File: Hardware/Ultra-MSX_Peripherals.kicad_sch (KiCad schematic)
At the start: 56 parts, among them J4 OST_Conn_302-S341, J5 Amphenol_L17H1220134, J6 DIN-8_SDF-80J, J7 AdamTech_USB3-2_USB_C_Recepta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, J8 SDF-130J, J9 Ultra-av-daughter, Q2 MMBT2907AM3T5G, U16 LM211

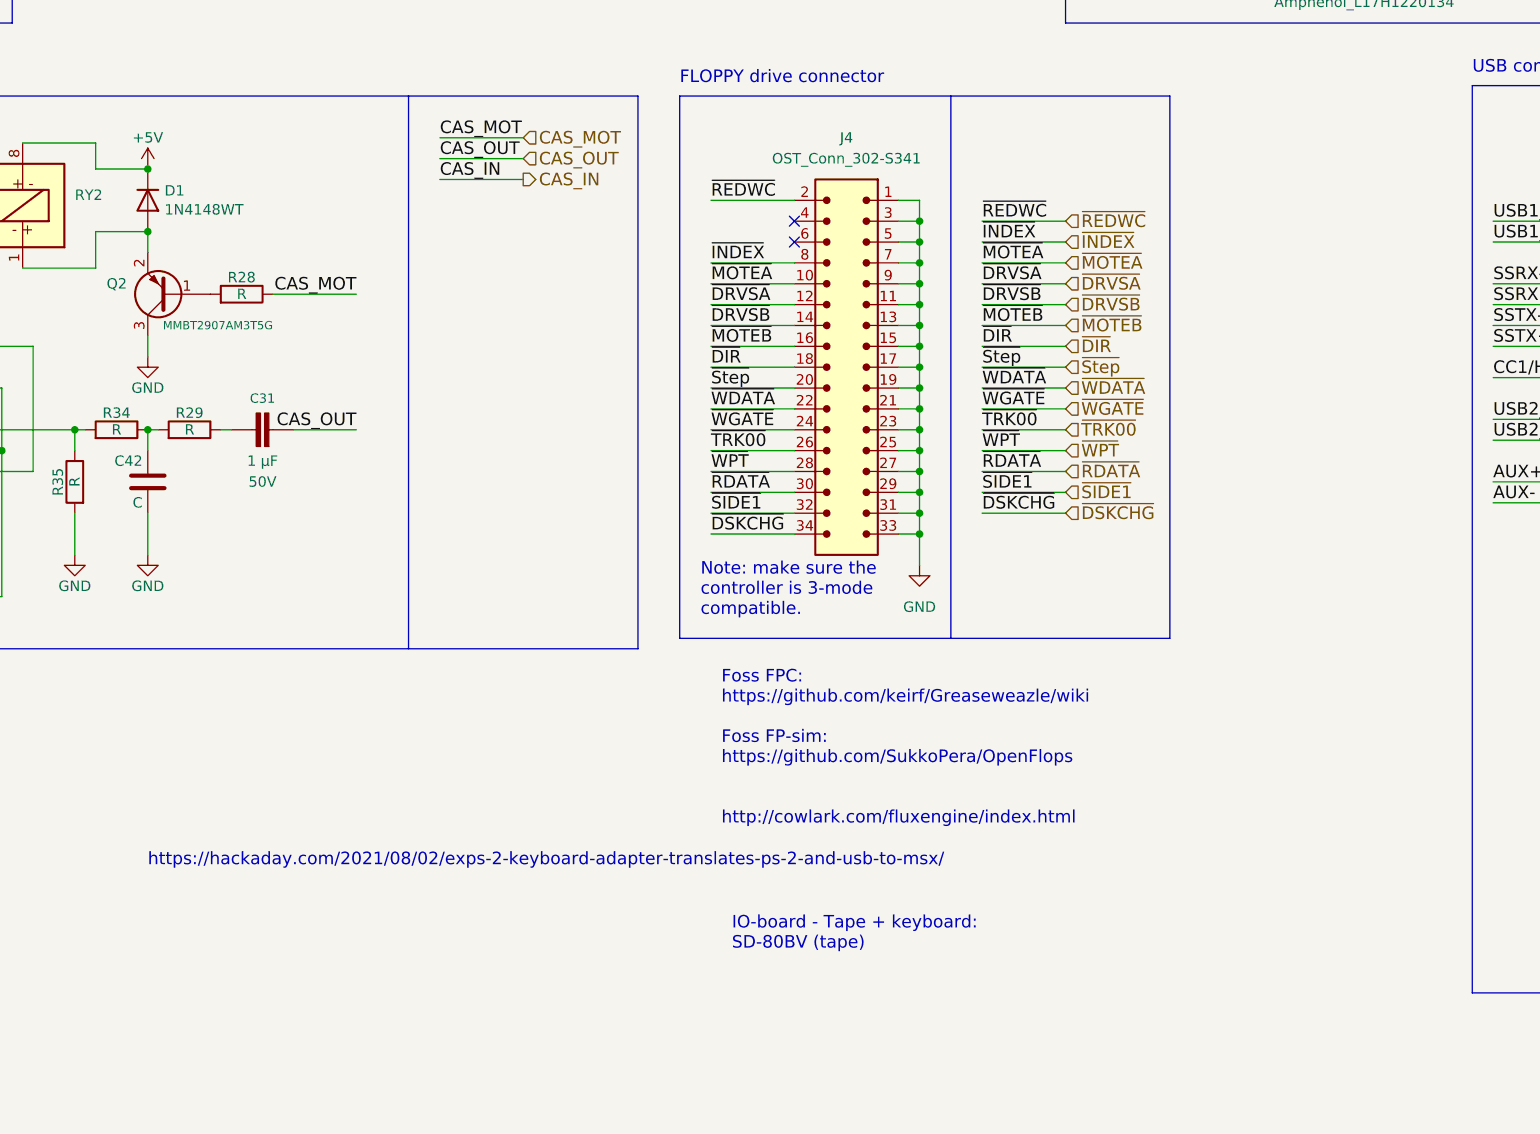
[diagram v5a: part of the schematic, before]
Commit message: Reworked the Printer-port 3D model, and the Scart 3D-model. Generated a 3D model of the main board. Moved peripheral components from separate expansion-headers, to a singular IO-shield board.
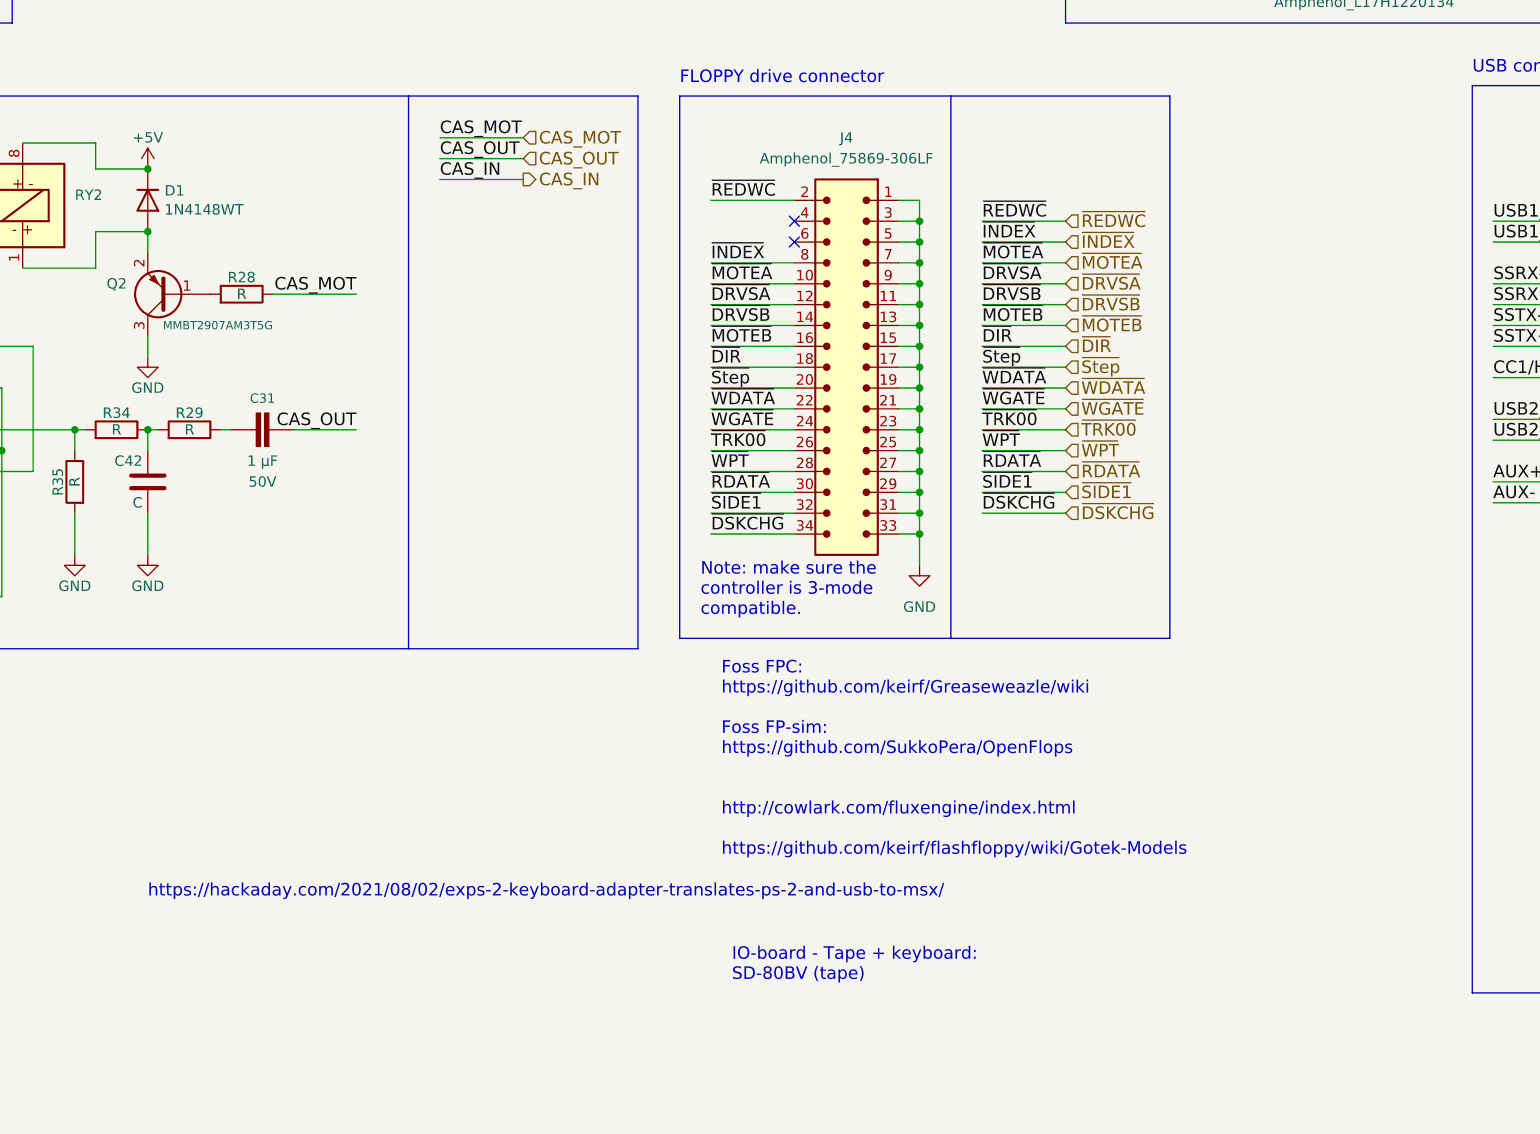
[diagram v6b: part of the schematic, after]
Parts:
- J4: value OST_Conn_302-S341 -> Amphenol_75869-306LF; footprint LRJ:OST_PinHeader_2x17_P2.54mm_Vertical -> LRJ:Amphenol_75869-306LF_2x17_P2.54mm_Vertical; symbol LRJ-parts:OST_Conn_302-S341 -> LRJ-parts:Amphenol_75869-306LF; MPN 302-S341 -> 75869-306LF; Manufacturer On Shore Technology Inc. -> Amphenol ICC (FCI); Operating Temperature (none) -> -65°C to +125°C
- J9: footprint Ultra-MSX:Ultra-video-daughter -> Ultra-MSX:Ultra-AV-daughter
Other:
- note added: "Foss FPC: https://github.com/keirf/Greaseweazle/wiki Foss FP-sim: https://github.com/SukkoPera/OpenFlops http://cowlark.com/fluxengine/index.html https://github.com/keirf/flashfloppy/wiki/Gotek-Models"
- note removed: "Foss FPC: https://github.com/keirf/Greaseweazle/wiki Foss FP-sim: https://github.com/SukkoPera/OpenFlops http://cowlark.com/fluxengine/index.html"
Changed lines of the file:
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@@
     (effects (font (size 1.524 1.524)) (justify left bottom))
   )
-  (text "IO-board - Tape + keyboard:\nSD-80BV (tape)\n" (at 217.17 199.39 0)
+  (text "IO-board - Tape + keyboard:\nSD-80BV (tape)\n" (at 217.17 203.2 0)
     (effects (font (size 1.524 1.524)) (justify left bottom))
   )
@@
     (effects (font (size 1.524 1.524)) (justify left bottom))
   )
-  (text "Foss FPC:\nhttps://github.com/keirf/Greaseweazle/wiki\n\nFoss FP-sim:\nhttps://github.com/SukkoPera/OpenFlops\n\n\nhttp://cowlark.com/fluxengine/index.html"
-    (at 215.9 184.15 0)
+  (text "Foss FPC:\nhttps://github.com/keirf/Greaseweazle/wiki\n\nFoss FP-sim:\nhttps://github.com/SukkoPera/OpenFlops\n\n\nhttp://cowlark.com/fluxengine/index.html\n\nhttps://github.com/keirf/flashfloppy/wiki/Gotek-Models"
+    (at 215.9 187.96 0)
     (effects (font (size 1.524 1.524)) (justify left bottom))
   )
@@
   )
   (text "https://hackaday.com/2021/08/02/exps-2-keyboard-adapter-translates-ps-2-and-usb-to-msx/"
-    (at 146.05 189.23 0)
+    (at 146.05 193.04 0)
     (effects (font (size 1.524 1.524)) (justify left bottom))
   )
@@
     (property "Reference" "J9" (id 0) (at 87.63 27.94 0))
     (property "Value" "Ultra-av-daughter" (id 1) (at 92.71 68.58 0))
-    (property "Footprint" "Ultra-MSX:Ultra-video-daughter" (id 2) (at 87.63 72.39 0)
+    (property "Footprint" "Ultra-MSX:Ultra-AV-daughter" (id 2) (at 87.63 72.39 0)
       (effects (font (size 1.27 1.27)) hide)
     )
@@
     (pin "9")
   )
-  (symbol (lib_id "LRJ-parts:OST_Conn_302-S341") (at 232.41 128.27 0) (mirror y) (unit 1)
+  (symbol (lib_id "LRJ-parts:Amphenol_75869-306LF") (at 232.41 128.27 0) (mirror y) (unit 1)
     (in_bom yes) (on_board yes) (fields_autoplaced)
     (property "Reference" "J4" (id 0) (at 231.14 100.33 0))
-    (property "Value" "OST_Conn_302-S341" (id 1) (at 231.14 102.87 0))
-    (property "Footprint" "LRJ:OST_PinHeader_2x17_P2.54mm_Vertical" (id 2) (at 229.87 156.21 0)
-      (effects (font (size 1.27 1.27)) hide)
-    )
-    (property "Datasheet" "http://www.on-shore.com/wp-content/uploads/2018/04/302-SXX1.pdf" (id 3) (at 181.61 135.89 0)
-      (effects (font (size 1.27 1.27)) hide)
-    )
-    (property "Mount" "THT" (id 4) (at 214.63 125.73 0)
-      (effects (font (size 1.27 1.27)) hide)
-    )
-    (property "Status" "Active" (id 5) (at 214.63 128.27 0)
-      (effects (font (size 1.27 1.27)) hide)
-    )
-    (property "Manufacturer" "On Shore Technology Inc." (id 6) (at 204.47 118.11 0)
-      (effects (font (size 1.27 1.27)) hide)
-    )
-    (property "MPN" "302-S341" (id 7) (at 212.09 120.65 0)
-      (effects (font (size 1.27 1.27)) hide)
-    )
-    (property "Description" "Connector Header THT 34 position 2.54mm" (id 8) (at 196.85 130.81 0)
+    (property "Value" "Amphenol_75869-306LF" (id 1) (at 231.14 102.87 0))
+    (property "Footprint" "LRJ:Amphenol_75869-306LF_2x17_P2.54mm_Vertical" (id 2) (at 229.87 156.21 0)
+      (effects (font (size 1.27 1.27)) hide)
+    )
+    (property "Datasheet" "https://cdn.amphenol-icc.com/media/wysiwyg/files/drawing/75869.pdf" (id 3) (at 181.61 143.51 0)
+      (effects (font (size 1.27 1.27)) hide)
+    )
+    (property "Mount" "THT" (id 4) (at 214.63 133.35 0)
+      (effects (font (size 1.27 1.27)) hide)
+    )
+    (property "Status" "Active" (id 5) (at 214.63 135.89 0)
+      (effects (font (size 1.27 1.27)) hide)
+    )
+    (property "Manufacturer" "Amphenol ICC (FCI)" (id 6) (at 204.47 118.11 0)
+      (effects (font (size 1.27 1.27)) hide)
+    )
+    (property "MPN" "75869-306LF" (id 7) (at 212.09 120.65 0)
+      (effects (font (size 1.27 1.27)) hide)
+    )
+    (property "Description" "Connector Header THT 34 position 2.54mm" (id 8) (at 196.85 138.43 0)
       (effects (font (size 1.27 1.27)) hide)
     )
@@
       (effects (font (size 1.27 1.27)) hide)
     )
+    (property "Operating Temperature" "-65°C to +125°C" (id 11) (at 209.55 128.27 0)
+      (effects (font (size 1.27 1.27)) hide)
+    )

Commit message: Redesigning of the IO-shield, to make room for Keyboard, power and USB.
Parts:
- removed C14, C84: C_GRM21BR71A106KA73K, Capacitor_SMD:C_0805_2012Metric_Pad1.18x1.45mm_HandSolder, symbol LRJ-parts:C_GRM21BR71A106KA73K
- removed C31: C_CL21B105KBFNNNF, Capacitor_SMD:C_0805_2012Metric_Pad1.18x1.45mm_HandSolder, symbol LRJ-parts:C_CL21B105KBFNNNF
- removed C40, C42, C71: C, Capacitor_SMD:C_0603_1608Metric, symbol Device:C
- removed D1: 1N4148WT, Diode_SMD:D_SOD-523, symbol Diode:1N4148WT
- removed F1: PPTC_SMD1812B075TF, Fuse:Fuse_1812_4532Metric, symbol LRJ-parts:PPTC_SMD1812B075TF
- removed J5: Amphenol_L17H1220134, LRJ:Amphenol_L17H1220134, symbol LRJ-parts:Amphenol_L17H1220134
- removed J6: DIN-8_SDF-80J, Ultra-MSX:Conn_DIN_8pin, symbol LRJ-parts:DIN-8_SDF-80J
- removed J8: SDF-130J, LRJ:DIN1648_R_13P_Female_Circular_Horizontal_THT, symbol LRJ-parts:SDF-130J
- removed J9: Ultra-av-daughter, Ultra-MSX:Ultra-AV-daughter, symbol Ultra-MSX:Ultra-av-daughter
- removed JP4: Jumper-KBD, Ultra-MSX:Conn_Pin_Header_2x1_2.54mm, symbol Ultra-MSX:Jumper-KBD
- removed Q2: MMBT2907AM3T5G, Package_TO_SOT_SMD:SOT-723, symbol LRJ-parts:MMBT2907AM3T5G
- removed R1, R78: R_ERJ-3GEYJ105V, Resistor_SMD:R_0603_1608Metric, symbol LRJ-parts:R_ERJ-3GEYJ105V
- removed R100, R101, R102, R103, R104, R105, R106, R107, R108, R109, R110, R111, R112, R113, R93, R94, R95, R96, R97, R98, R99: R_RC0603FR-074K7L, Resistor_SMD:R_0603_1608Metric, symbol LRJ-parts:R_RC0603FR-074K7L
- removed R28, R29, R34, R35, R40, R41, R42, R43, R45, R46, R48: R, Resistor_SMD:R_0603_1608Metric, symbol Device:R
- removed R47: R, Resistor_SMD:R_0805_2012Metric, symbol Device:R
- removed RY2: TE_IM43GR, LRJ:Relay_DPDT_AXICOM_IMSeries_GullWing, symbol LRJ-parts:TE_IM43GR
- removed U16: LM211, Package_SO:SOIC-8_3.9x4.9mm_P1.27mm, symbol LRJ-parts:LM211
- added C12: C_GRM21BR71A106KA73K, Capacitor_SMD:C_0805_2012Metric_Pad1.18x1.45mm_HandSolder, symbol LRJ-parts:C_GRM21BR71A106KA73K
- added J5: Ultra-IO-shield, Ultra-MSX:Ultra-IO-shield, symbol Ultra-MSX:Ultra-IO-shield
- added J6: SDF-130J, LRJ:DIN1648_R_13P_Female_Circular_Horizontal_THT, symbol LRJ-parts:SDF-130J
- added JP1: Jumper-KBD, Ultra-MSX:Conn_Pin_Header_2x1_2.54mm, symbol Ultra-MSX:Jumper-KBD
- added R1, R28, R29, R34, R35, R39, R40, R41, R42: R_RC0603FR-074K7L, Resistor_SMD:R_0603_1608Metric, symbol LRJ-parts:R_RC0603FR-074K7L
- added R43: R_ERJ-3GEYJ105V, Resistor_SMD:R_0603_1608Metric, symbol LRJ-parts:R_ERJ-3GEYJ105V
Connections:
- net +5V: now also C12.1, J6.12, R1.2, R28.2, R29.2, R34.2, R35.2, R39.2, R40.2, R41.2, R42.2
- net CAPS_LED: now also J6.2
- net COL0: now also J6.3, R1.1
- net COL1: now also J6.4, R28.1
- net COL2: now also J6.5, R29.1
- net COL3: now also J6.6, R34.1
- net COL4: now also J6.7, R35.1
- net COL5: now also J6.8, R39.1
- net COL6: now also J6.9, R40.1
- net COL7: now also J6.10, R41.1
- net GND: now also C12.2, J6.13, JP1.2, R43.2
- net KANA_LED: now also J6.1
- net KBD_TYPE: now also JP1.1, R42.1
- net KEY_DIR: now also J6.11
- new net: J6.SH, R43.1
- no-connect marks 15 -> 9
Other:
- note removed: "Cassette I/O (optional)"
- note removed: "JOYSTICKS"
- note removed: "Joystick Pull-ups"
- note removed: "PRINTER"
- note removed: "See 'Ultra-AV' daughter-card for schematics on connector."
- note removed: "ULTRA-AV daughter-card"
- moved on the sheet: J4, R79

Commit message: Multiple redesigns of the IO-shield. Replaced FPGA with lower pin-count AT10K, since the higher pin-count one is now obsolete.
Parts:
- removed C29: C_GRM21BR61A476ME15K, Capacitor_SMD:C_0805_2012Metric, symbol LRJ-parts:C_GRM21BR61A476ME15K
- removed J7: AdamTech_USB3-2_USB_C_Receptacle, LRJ:USB_3-2_Receptacle_A3-C31-D-RA-CS1, symbol LRJ-parts:AdamTech_USB3-2_USB_C_Receptacle
- removed R19: R_ERJ-3GEYJ105V, Resistor_SMD:R_0603_1608Metric, symbol LRJ-parts:R_ERJ-3GEYJ105V
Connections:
- net +5V: now also J5.14 (+5V), J5.23 (+5V), J5.37 (+5V)
- net AUD_L: now also J5.52 (AUD_L)
- net AUD_R: now also J5.53 (AUD_R)
- net BOUT: now also J5.51 (BOUT)
- net CAS_IN: now also J5.3 (CAS_IN)
- net CAS_MOT: now also J5.2 (CAS_MOT)
- net CAS_OUT: now also J5.1 (CAS_OUT)
- net CC1/HPD: now also J5.35 (CC1/HPD)
- net CSYNC: now also J5.50 (CSYNC)
- net GND: now also J5.22 (GND), J5.30 (GND), J5.36 (GND)
- net GOUT: now also J5.49 (GOUT)
- net JOY_OUT_A: now also J5.8 (JOY_OUT_A)
- net JOY_OUT_B: now also J5.16 (JOY_OUT_B)
- net PD0: now also J5.46 (PD0)
- net PD1: now also J5.45 (PD1)
- net PD2: now also J5.44 (PD2)
- net PD3: now also J5.43 (PD3)
- net PD4: now also J5.42 (PD4)
- net PD5: now also J5.40 (PD5)
- net PD6: now also J5.41 (PD6)
- net PD7: now also J5.39 (PD7)
- net PRT_BUSY: now also J5.38 (PRT_BUSY)
- net ROUT: now also J5.48 (ROUT)
- net RX1+: now also J5.27 (RX1+)
- net RX1-: now also J5.26 (RX1-)
- net USB1_D+: now also J5.29 (USB1_D+)
- net USB1_D-: now also J5.28 (USB1_D-)
- net USB2_D+: now also J5.32 (USB2_D+)
- net USB2_D-: now also J5.31 (USB2_D-)
- net ~{BCK_A}: now also J5.11 (~{BCK_A})
- net ~{BCK_B}: now also J5.18 (~{BCK_B})
- net ~{FWD_A}: now also J5.21 (~{FWD_A})
- net ~{FWD_B}: now also J5.13 (~{FWD_B})
- net ~{LFT_A}: now also J5.10 (~{LFT_A})
- net ~{LFT_B}: now also J5.17 (~{LFT_B})
- net ~{RGT_A}: now also J5.7 (~{RGT_A})
- net ~{RGT_B}: now also J5.15 (~{RGT_B})
- net ~{STROBE}: now also J5.47 (~{STROBE})
- net ~{TRG1_A}: now also J5.12 (~{TRG1_A})
- net ~{TRG1_B}: now also J5.20 (~{TRG1_B})
- net ~{TRG2_A}: now also J5.9 (~{TRG2_A})
- net ~{TRG2_B}: now also J5.19 (~{TRG2_B})
- net +12V: now reaches J5.4 (+12V)
- net MID_TX: now reaches J5.5 (MID_TX)
- net MID_RX: now reaches J5.6 (MID_RX)
- new net GNDA: J5.54 (GNDA), J5.55 (GNDA)
- new net RX2+: J5.34 (RX2+)
- new net RX2-: J5.33 (RX2-)
- new net SBU1/AUX1+: J5.24 (AUX1+)
- new net SBU2/AUX1-: J5.25 (AUX2-)
- no-connect marks 9 -> 2
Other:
- note added: "AUDIO-nets"
- note added: "CASSETTE-nets"
- note added: "IO-SHIELD daughter-card (see separate schematic for more details)"
- note added: "Joysticks"
- note added: "KEYBOARD-nets"
- note added: "MIDI-nets"
- note added: "PRINTER"
- note added: "PRINTER-nets"
- note added: "Representative symbol for the connections to the IO-shield -card."
- note added: "USB connectors"
- note added: "VIDEO-nets"
- note removed: "USB connector"
- moved on the sheet: C12, J4, J6, JP1, R1, R28, R29, R34, R35, R39, R40, R41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
